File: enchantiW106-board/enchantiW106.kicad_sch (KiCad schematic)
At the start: 71 parts, among them J1 USB_C_Receptacle_USB2.0, SW1 B3U-1000P, SW2 B3U-1000P, U1 USBLC6-2P6, U11 MAX17262REWL+T, U12 BQ25185DLHR, U13 ICM-42670-P, U2 MMC5633NJL, U3 IRIS-W106-00B, U4 NCP167AMX330TBG, U5 CP2102N-Axx-xQFN20, U9 NCP167AMX330TBG

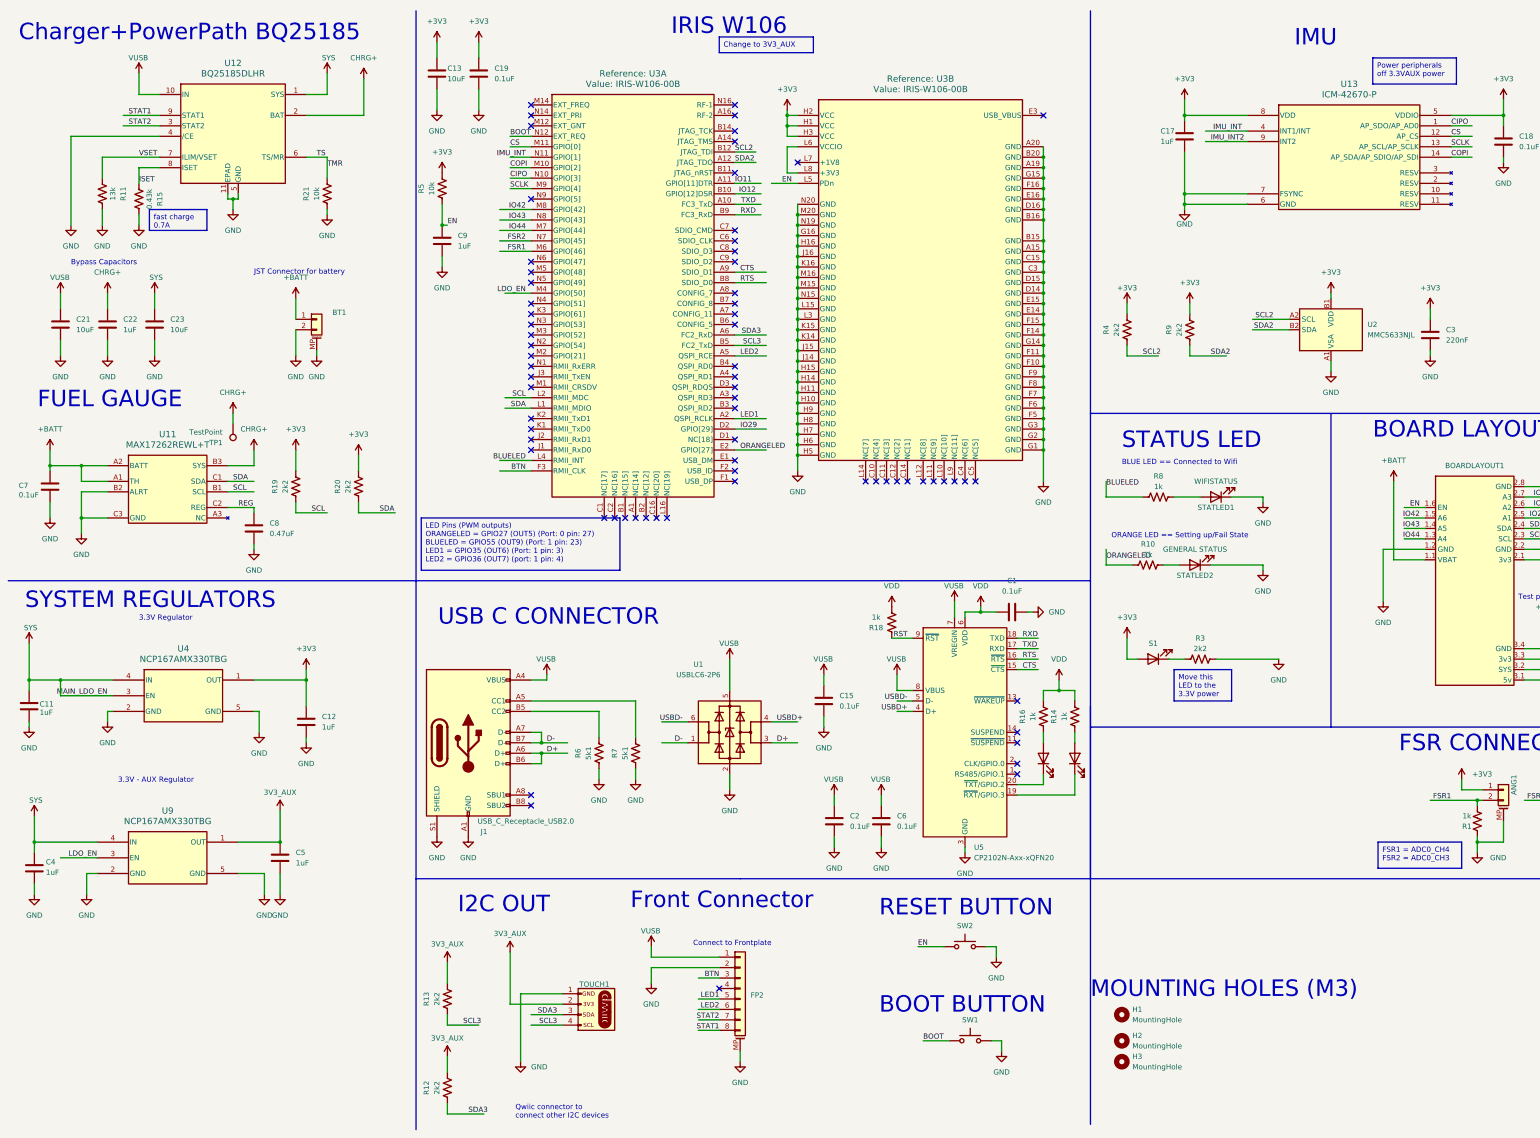
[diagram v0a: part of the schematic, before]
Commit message: changed board width to 31.75mm, remove unused components
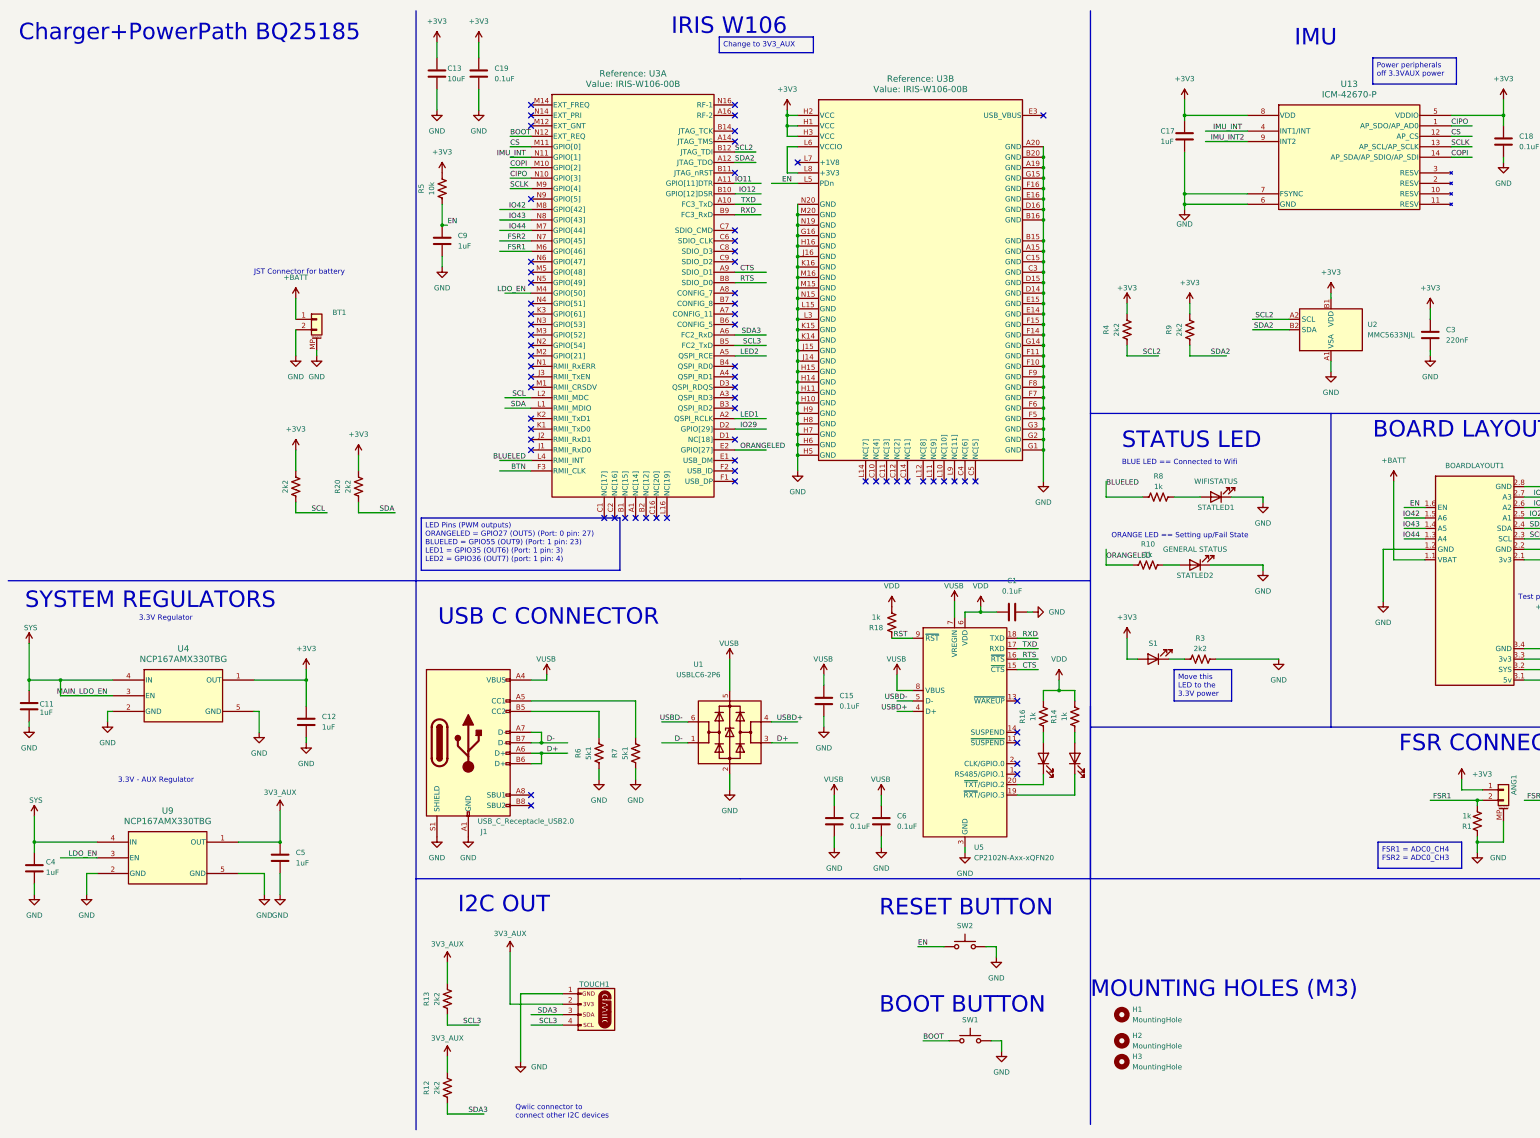
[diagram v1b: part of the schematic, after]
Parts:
- removed C21, C23: 10uF, Capacitor_SMD:C_0603_1608Metric, symbol Device:C
- removed C22: 1uF, Capacitor_SMD:C_0402_1005Metric, symbol Device:C
- removed C7: 0.1uF, Capacitor_SMD:C_0402_1005Metric, symbol Device:C
- removed C8: 0.47uF, Capacitor_SMD:C_0402_1005Metric, symbol Device:C
- removed FP2: CONN HEADER SMD 6POS 1MM, Connector_Molex:Molex_Pico-Clasp_501331-0807_1x08-1MP_P1.00mm_Vertical, symbol ENCHANTI_connectors:PicoClasp_8pin
- removed R11: 13k, Resistor_SMD:R_0402_1005Metric, symbol Device:R_US
- removed R15: 0.43k, Resistor_SMD:R_0402_1005Metric, symbol Device:R_US
- removed R21: 10k, Resistor_SMD:R_0402_1005Metric, symbol Device:R_US
- removed SYS1, SYS8: SYS, symbol power-symbols:VSYS
- removed TP1: TestPoint, TestPoint:TestPoint_Pad_D1.0mm, symbol Connector:TestPoint
- removed U11: MAX17262REWL+T, ENCHANTI_battery-management:MAX17262, symbol ENCHANTI_battery-management:MAX17262REWL+T
- removed U12: BQ25185DLHR, ENCHANTI_battery-management:WSON10_DLH_TEX, symbol ENCHANTI_battery-management:BQ25185DLHR
- BOARDLAYOUT1: footprint ENCHANTI_enchanti-board-symbols:enchantiS3-layout -> ENCHANTI_enchanti-board-symbols:enchantiW106-layout
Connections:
- no-connect marks 70 -> 69
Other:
- note removed: "Bypass Capacitors"
- note removed: "Connect to Frontplate"
- note removed: "FUEL GAUGE"
- note removed: "Front Connector"

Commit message: Begin rearranging MCU board to have a coprocessor
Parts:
- removed ANG1, ANG3: CONN HEADER SMD 2POS 1MM, ENCHANTI_connectors:Molex_Pico-Clasp_2pin_Vertical, symbol ENCHANTI_connectors:PicoClasp_2pin
- removed BOARDLAYOUT1: LAYOUT, ENCHANTI_enchanti-board-symbols:enchantiW106-layout, symbol pin-layout:board-layout
- removed BT1: JST-PH-1x02-2.000mm, Connector_JST:JST_PH_S2B-PH-SM4-TB_1x02-1MP_P2.00mm_Horizontal, symbol Connector_Generic_MountingPin:Conn_01x02_MountingPin
- removed C1, C15, C18, C19, C2, C6: 0.1uF, Capacitor_SMD:C_0402_1005Metric, symbol Device:C
- removed C11, C12, C17, C4, C5, C9: 1uF, Capacitor_SMD:C_0402_1005Metric, symbol Device:C
- removed C13: 10uF, Capacitor_SMD:C_0603_1608Metric, symbol Device:C
- removed C3: 220nF, Capacitor_SMD:C_0402_1005Metric, symbol Device:C
- removed CHARGLED1: S1, LED_SMD:LED_0402_1005Metric, symbol Device:LED
- removed H1, H2, H3: MountingHole, MountingHole:MountingHole_2.2mm_M2, symbol Mechanical:MountingHole
- removed J1: USB_C_Receptacle_USB2.0, Connector_USB:USB_C_Receptacle_GCT_USB4105-xx-A_16P_TopMnt_Horizontal, symbol Connector:USB_C_Receptacle_USB2.0
- removed R1, R10, R14, R16, R18, R2, R8: 1k, Resistor_SMD:R_0402_1005Metric, symbol Device:R_US
- removed R12, R13, R19, R20, R3, R4, R9: 2k2, Resistor_SMD:R_0402_1005Metric, symbol Device:R_US
- removed R5: 10k, Resistor_SMD:R_0402_1005Metric, symbol Device:R_US
- removed R6, R7: 5k1, Resistor_SMD:R_0402_1005Metric, symbol Device:R_US
- removed STATLED1: WIFISTATUS, LED_SMD:LED_0402_1005Metric, symbol Device:LED
- removed STATLED2: GENERAL STATUS, LED_SMD:LED_0402_1005Metric, symbol Device:LED
- removed STATLED3: TX_STAT, LED_SMD:LED_0402_1005Metric, symbol Device:LED
- removed STATLED4: RX_STAT, LED_SMD:LED_0402_1005Metric, symbol Device:LED
- removed SW1, SW2: B3U-1000P, Button_Switch_SMD:SW_SPST_B3U-1000P, symbol Switch:SW_Push
- removed SYS2, SYS4, SYS6: SYS, symbol power-symbols:VSYS
- removed TOUCH1: JST-SH-1x04 1.0mm, ENCHANTI_connectors:JST_SMD_1.0mm-4_Vertical, symbol ENCHANTI_connectors:QWIIC-CONNECTOR
- removed U1: USBLC6-2P6, Package_TO_SOT_SMD:SOT-666, symbol Power_Protection:USBLC6-2P6
- removed U13: ICM-42670-P, ENCHANTI_MEMS:LGA14_2P5X3X0P91_TDK, symbol ENCHANTI_mems:ICM-42670-P
- removed U2: MMC5633NJL, Package_BGA:WLP-4_0.86x0.86mm_P0.4mm, symbol Sensor_Magnetic:MMC5633NJL
- removed U3: IRIS-W106-00B, ENCHANTI_WiFi:IRIS-W106, symbol ENCHANTI_wifi:IRIS-W106
- removed U4, U9: NCP167AMX330TBG, ENCHANTI_regulators:XDFN4_1X1_711AJ_ONS, symbol ENCHANTI_regulators:NCP167AMX330TBG
- removed U5: CP2102N-Axx-xQFN20, Package_DFN_QFN:SiliconLabs_QFN-20-1EP_3x3mm_P0.5mm_EP1.8x1.8mm, symbol Interface_USB:CP2102N-Axx-xQFN20
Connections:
- no-connect marks 69 -> 0
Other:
- added sheet Battery and Power Management (subschematics/power.kicad_sch)
- added sheet Iris W106 (subschematics/mcu.kicad_sch)
- added sheet Peripherals (subschematics/peripherals.kicad_sch)
- added sheet Sensor Co-Processor (subschematics/coprocessor.kicad_sch)
- added sheet USB-UART Bridge (subschematics/usb_uart.kicad_sch)
- note removed: "3.3V - AUX Regulator"
- note removed: "3.3V Regulator"
- note removed: "BLUE LED == Connected to Wifi"
- note removed: "BOARD LAYOUT"
- note removed: "BOOT BUTTON"
- note removed: "Charger+PowerPath BQ25185"
- note removed: "FSR CONNECTOR"
- note removed: "I2C OUT"
- note removed: "IMU"
- note removed: "IRIS W106"
- note removed: "JST Connector for battery"
- note removed: "MOUNTING HOLES (M3)"
- note removed: "ORANGE LED == Setting up/Fail State"
- note removed: "Qwiic connector to connect other I2C devices"
- note removed: "RESET BUTTON"
- note removed: "STATUS LED"
- note removed: "SYSTEM REGULATORS"
- note removed: "Test point for current measurement"
- note removed: "USB C CONNECTOR"
- title: Custom T-Stick Board -> EnchantiW106
